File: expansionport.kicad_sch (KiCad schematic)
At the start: 18 parts, among them J20 C64_Expansion_Port, U31 74LS04, U32 74LVC374, U33 74LVC374, U34 74LVC374, U35 74LS374, U36 74LS374, U37 74LS374, U38 74LVC374, U39 74LVC374, U40 74LS374, U41 74LS374, U42 74LS06

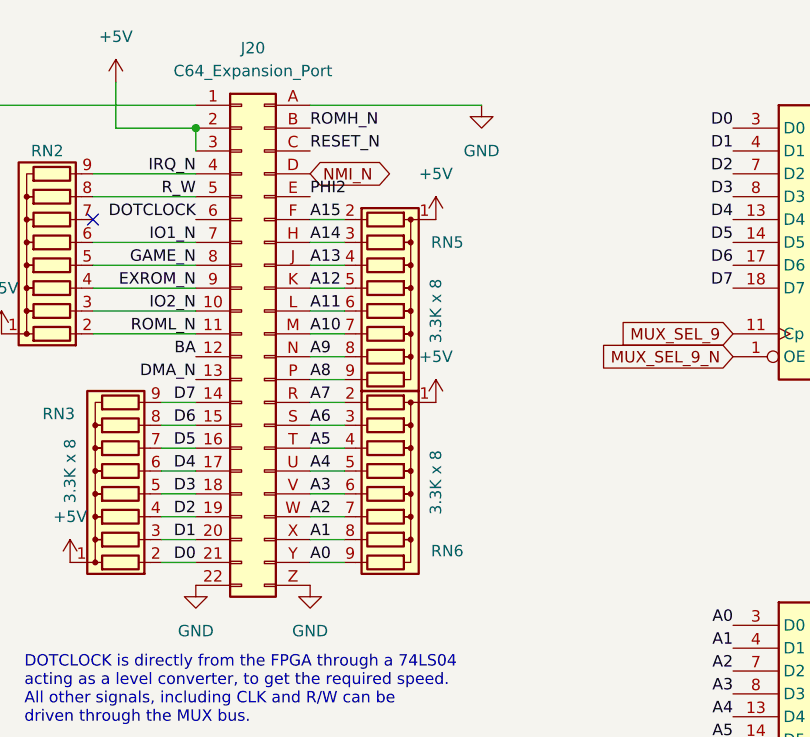
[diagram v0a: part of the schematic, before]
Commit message: route joystick ports and pullups etc
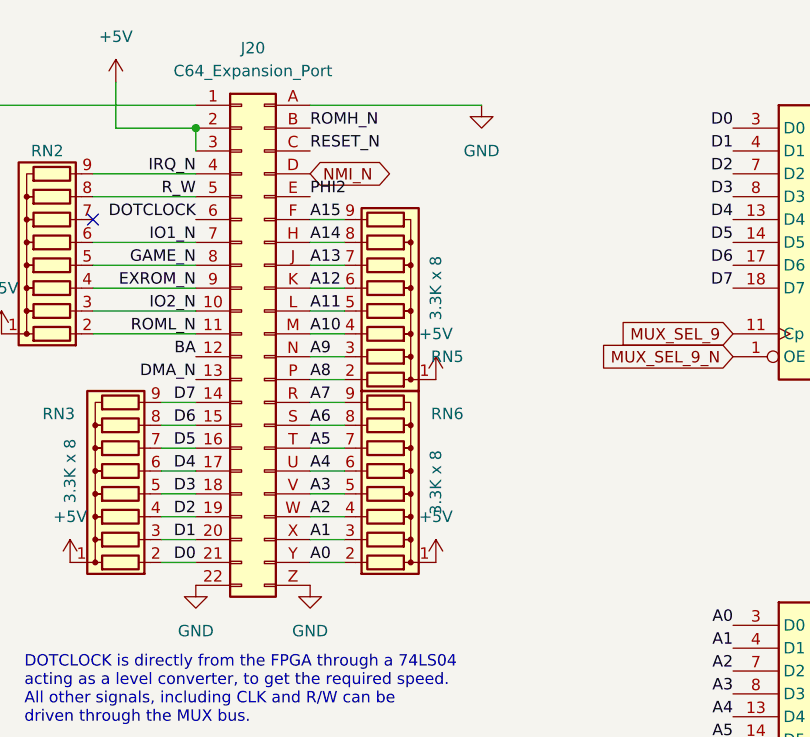
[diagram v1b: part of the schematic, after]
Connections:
- net A0: now also RN6.2 (R1); no longer RN6.9 (R8)
- net A1: now also RN6.3 (R2); no longer RN6.8 (R7)
- net A10: now also RN5.4 (R3); no longer RN5.7 (R6)
- net A11: now also RN5.5 (R4); no longer RN5.6 (R5)
- net A12: now also RN5.6 (R5); no longer RN5.5 (R4)
- net A13: now also RN5.7 (R6); no longer RN5.4 (R3)
- net A14: now also RN5.8 (R7); no longer RN5.3 (R2)
- net A15: now also RN5.9 (R8); no longer RN5.2 (R1)
- net A2: now also RN6.4 (R3); no longer RN6.7 (R6)
- net A3: now also RN6.5 (R4); no longer RN6.6 (R5)
- net A4: now also RN6.6 (R5); no longer RN6.5 (R4)
- net A5: now also RN6.7 (R6); no longer RN6.4 (R3)
- net A6: now also RN6.8 (R7); no longer RN6.3 (R2)
- net A7: now also RN6.9 (R8); no longer RN6.2 (R1)
- net A8: now also RN5.2 (R1); no longer RN5.9 (R8)
- net A9: now also RN5.3 (R2); no longer RN5.8 (R7)
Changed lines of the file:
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@@
     (pin "1")
   )
-  (symbol (lib_id "Device:R_Network08") (at 66.04 69.85 270) (unit 1)
+  (symbol (lib_id "Device:R_Network08") (at 66.04 67.31 270) (mirror x) (unit 1)
     (in_bom yes) (on_board yes)
-    (property "Reference" "RN6" (id 0) (at 72.39 76.2 90))
+    (property "Reference" "RN6" (id 0) (at 72.39 60.96 90))
     (property "Value" "3.3K x 8" (id 1) (at 71.12 68.58 0))
-    (property "Footprint" "Resistor_THT:R_Array_SIP9" (id 2) (at 66.04 81.915 90)
-      (effects (font (size 1.27 1.27)) hide)
-    )
-    (property "Datasheet" "http://www.vishay.com/docs/31509/csc.pdf" (id 3) (at 66.04 69.85 0)
+    (property "Footprint" "Resistor_THT:R_Array_SIP9" (id 2) (at 66.04 55.245 90)
+      (effects (font (size 1.27 1.27)) hide)
+    )
+    (property "Datasheet" "http://www.vishay.com/docs/31509/csc.pdf" (id 3) (at 66.04 67.31 0)
       (effects (font (size 1.27 1.27)) hide)
     )
@@
     (pin "Z")
   )
-  (symbol (lib_id "Device:R_Network08") (at 66.04 49.53 270) (unit 1)
+  (symbol (lib_id "Device:R_Network08") (at 66.04 46.99 270) (mirror x) (unit 1)
     (in_bom yes) (on_board yes)
-    (property "Reference" "RN5" (id 0) (at 72.39 41.91 90))
-    (property "Value" "3.3K x 8" (id 1) (at 71.12 49.53 0))
-    (property "Footprint" "Resistor_THT:R_Array_SIP9" (id 2) (at 66.04 61.595 90)
-      (effects (font (size 1.27 1.27)) hide)
-    )
-    (property "Datasheet" "http://www.vishay.com/docs/31509/csc.pdf" (id 3) (at 66.04 49.53 0)
+    (property "Reference" "RN5" (id 0) (at 72.39 54.61 90))
+    (property "Value" "3.3K x 8" (id 1) (at 71.12 46.99 0))
+    (property "Footprint" "Resistor_THT:R_Array_SIP9" (id 2) (at 66.04 34.925 90)
+      (effects (font (size 1.27 1.27)) hide)
+    )
+    (property "Datasheet" "http://www.vishay.com/docs/31509/csc.pdf" (id 3) (at 66.04 46.99 0)
       (effects (font (size 1.27 1.27)) hide)
     )
@@
     (pin "1")
   )
-  (symbol (lib_id "power:+5V") (at 71.12 59.69 0) (unit 1)
-    (in_bom yes) (on_board yes) (fields_autoplaced)
-    (property "Reference" "#PWR0238" (id 0) (at 71.12 63.5 0)
-      (effects (font (size 1.27 1.27)) hide)
-    )
-    (property "Value" "+5V" (id 1) (at 71.12 54.61 0))
-    (property "Footprint" "" (id 2) (at 71.12 59.69 0)
-      (effects (font (size 1.27 1.27)) hide)
-    )
-    (property "Datasheet" "" (id 3) (at 71.12 59.69 0)
+  (symbol (lib_id "power:+5V") (at 71.12 77.47 0) (unit 1)
+    (in_bom yes) (on_board yes) (fields_autoplaced)
+    (property "Reference" "#PWR0238" (id 0) (at 71.12 81.28 0)
+      (effects (font (size 1.27 1.27)) hide)
+    )
+    (property "Value" "+5V" (id 1) (at 71.12 72.39 0))
+    (property "Footprint" "" (id 2) (at 71.12 77.47 0)
+      (effects (font (size 1.27 1.27)) hide)
+    )
+    (property "Datasheet" "" (id 3) (at 71.12 77.47 0)
       (effects (font (size 1.27 1.27)) hide)
     )
@@
     (pin "1")
   )
-  (symbol (lib_id "power:+5V") (at 71.12 39.37 0) (unit 1)
-    (in_bom yes) (on_board yes) (fields_autoplaced)
-    (property "Reference" "#PWR0248" (id 0) (at 71.12 43.18 0)
-      (effects (font (size 1.27 1.27)) hide)
-    )
-    (property "Value" "+5V" (id 1) (at 71.12 34.29 0))
-    (property "Footprint" "" (id 2) (at 71.12 39.37 0)
-      (effects (font (size 1.27 1.27)) hide)
-    )
-    (property "Datasheet" "" (id 3) (at 71.12 39.37 0)
-      (effects (font (size 1.27 1.27)) hide)
-    )
+  (symbol (lib_id "power:+5V") (at 71.12 57.15 0) (unit 1)
+    (in_bom yes) (on_board yes) (fields_autoplaced)
+    (property "Reference" "#PWR0248" (id 0) (at 71.12 60.96 0)
+      (effects (font (size 1.27 1.27)) hide)
+    )
+    (property "Value" "+5V" (id 1) (at 71.12 52.07 0))
+    (property "Footprint" "" (id 2) (at 71.12 57.15 0)
+      (effects (font (size 1.27 1.27)) hide)
+    )
+    (property "Datasheet" "" (id 3) (at 71.12 57.15 0)
+      (effects (font (size 1.27 1.27)) hide)
+    )

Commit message: add missing footprints
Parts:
- U42: footprint (none) -> Package_DIP:DIP-14_W7.62mm
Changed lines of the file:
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@@
       (effects (font (size 1.27 1.27)) (justify left))
     )
-    (property "Footprint" "" (id 2) (at 19.05 176.53 0)
+    (property "Footprint" "Package_DIP:DIP-14_W7.62mm" (id 2) (at 19.05 176.53 0)
       (effects (font (size 1.27 1.27)) hide)
     )
@@
     (property "Reference" "U42" (id 0) (at 45.085 179.07 0))
     (property "Value" "74LS06" (id 1) (at 45.085 181.61 0))
-    (property "Footprint" "" (id 2) (at 45.085 187.96 0)
+    (property "Footprint" "Package_DIP:DIP-14_W7.62mm" (id 2) (at 45.085 187.96 0)
       (effects (font (size 1.27 1.27)) hide)
     )
@@
     (property "Reference" "U42" (id 0) (at 90.805 167.64 0))
     (property "Value" "74LS06" (id 1) (at 90.805 170.18 0))
-    (property "Footprint" "" (id 2) (at 90.805 177.165 0)
+    (property "Footprint" "Package_DIP:DIP-14_W7.62mm" (id 2) (at 90.805 177.165 0)
       (effects (font (size 1.27 1.27)) hide)
     )
@@
     (property "Reference" "U42" (id 0) (at 90.805 179.07 0))
     (property "Value" "74LS06" (id 1) (at 90.805 181.61 0))
-    (property "Footprint" "" (id 2) (at 90.805 187.96 0)
+    (property "Footprint" "Package_DIP:DIP-14_W7.62mm" (id 2) (at 90.805 187.96 0)
       (effects (font (size 1.27 1.27)) hide)
     )
@@
     (property "Reference" "U42" (id 0) (at 41.91 151.765 0))
     (property "Value" "74LS06" (id 1) (at 41.91 154.305 0))
-    (property "Footprint" "" (id 2) (at 41.91 161.29 0)
+    (property "Footprint" "Package_DIP:DIP-14_W7.62mm" (id 2) (at 41.91 161.29 0)
       (effects (font (size 1.27 1.27)) hide)
     )
@@
     (property "Reference" "U42" (id 0) (at 138.43 179.07 0))
     (property "Value" "74LS06" (id 1) (at 138.43 181.61 0))
-    (property "Footprint" "" (id 2) (at 138.43 187.96 0)
+    (property "Footprint" "Package_DIP:DIP-14_W7.62mm" (id 2) (at 138.43 187.96 0)
       (effects (font (size 1.27 1.27)) hide)
     )
@@
     (property "Reference" "U42" (id 0) (at 138.43 167.64 0))
     (property "Value" "74LS06" (id 1) (at 138.43 170.18 0))
-    (property "Footprint" "" (id 2) (at 138.43 177.165 0)
-      (effects (font (size 1.27 1.27)) hide)
-    )
+    (property "Footprint" "Package_DIP:DIP-14_W7.62mm" (id 2) (at 138.43 177.165 0)
+      (effects (font (size 1.27 1.27)) hide)
+    )

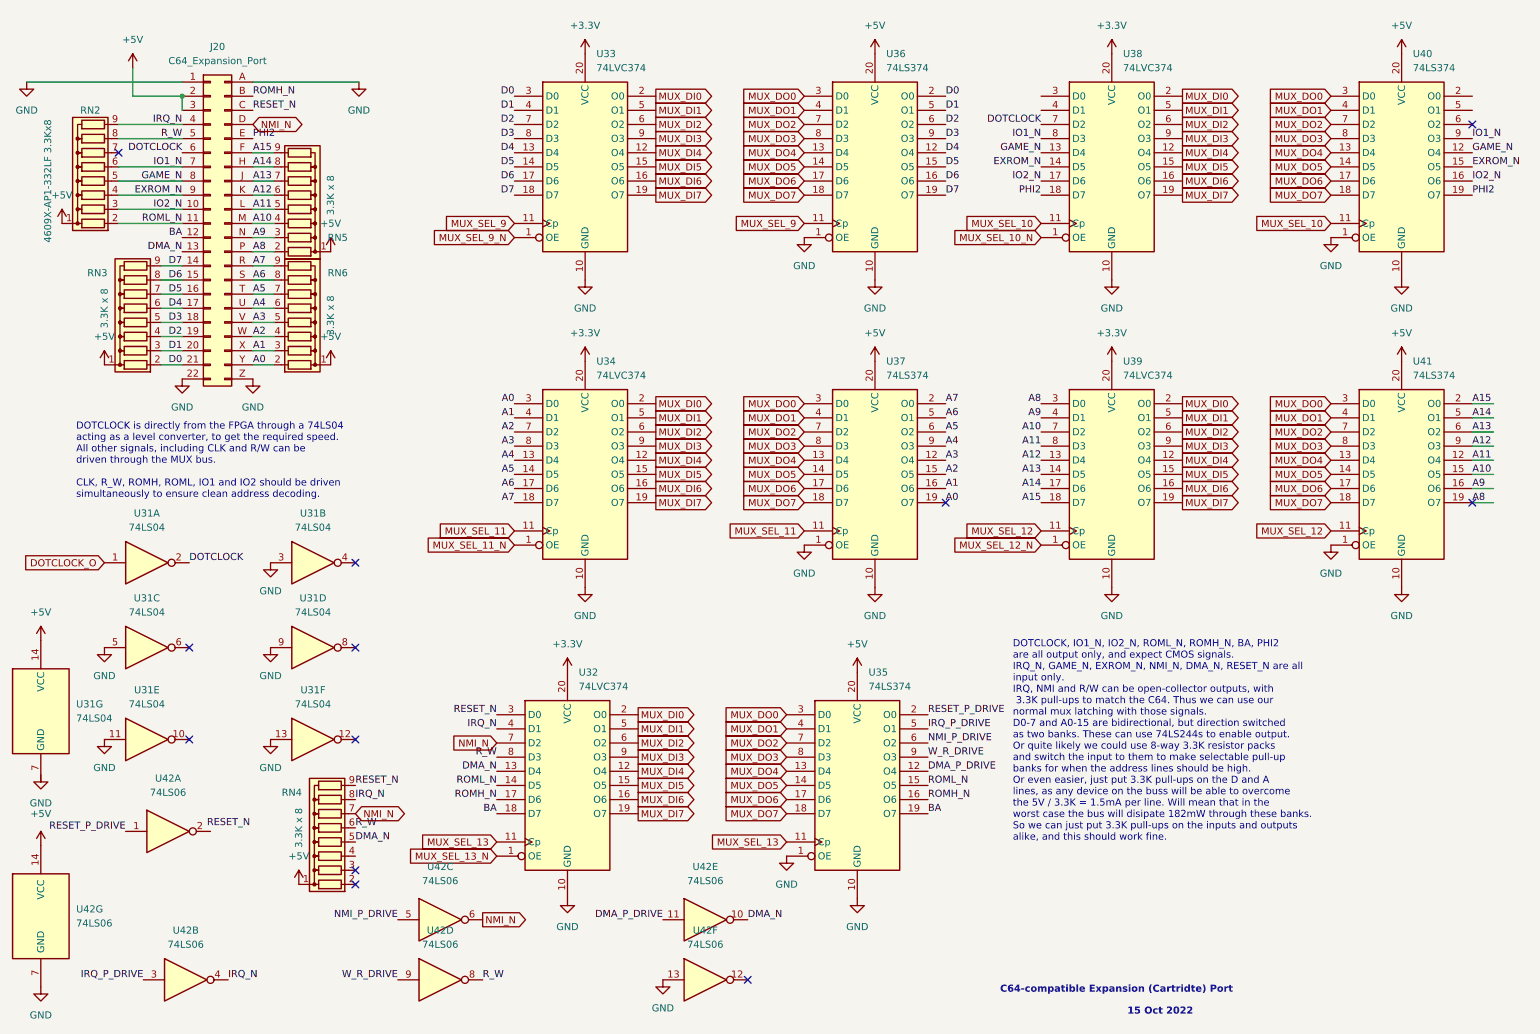
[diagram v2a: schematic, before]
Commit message: route cart port to resistor packs
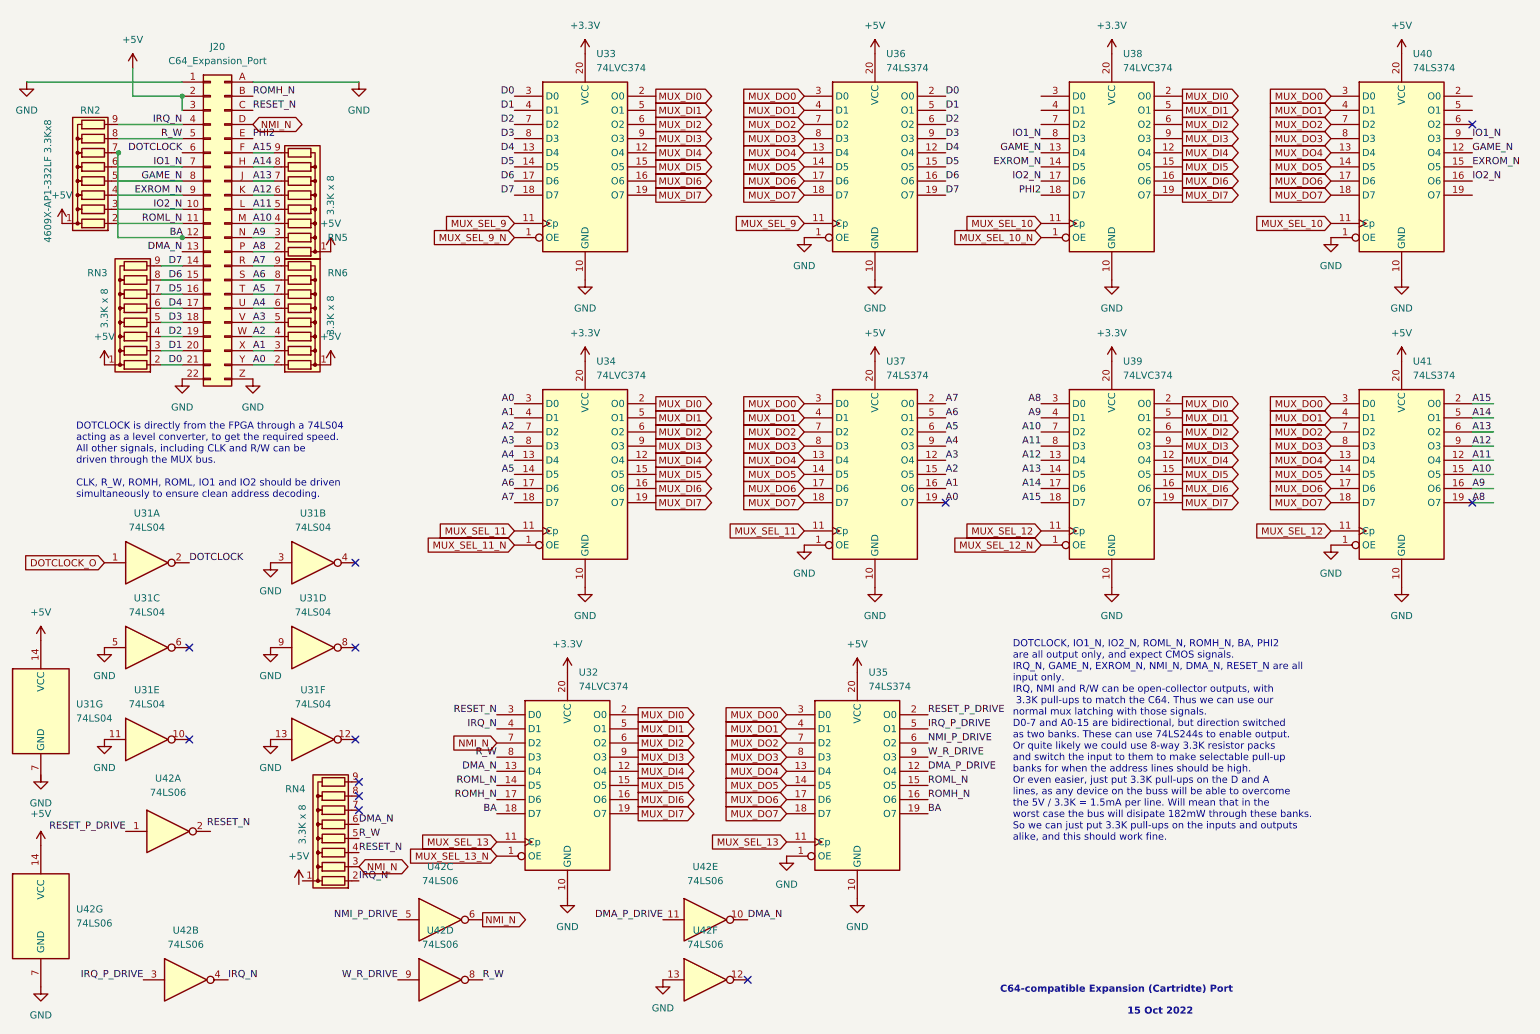
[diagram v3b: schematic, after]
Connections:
- net +5V: no longer RN4.1 (common)
- net BA: now also RN2.7 (R6)
- net DMA_N: now also RN4.6 (R5); no longer RN4.5 (R4)
- net DOTCLOCK: no longer U38.7 (D2)
- net IRQ_N: now also RN4.2 (R1); no longer RN4.8 (R7)
- net NMI_N: now also RN4.3 (R2); no longer RN4.7 (R6)
- net PHI2: no longer U40.19 (O7)
- net RESET_N: now also RN4.4 (R3); no longer RN4.9 (R8)
- net R_W: now also RN4.5 (R4); no longer RN4.6 (R5)
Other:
- moved on the sheet: RN4
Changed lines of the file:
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@@
 (kicad_sch (version 20211123) (generator eeschema)
   (paper "A4")
+  (junction (at 44.45 54.61) (diameter 0) (color 0 0 0 0)
+  )
+  (junction (at 33.02 39.37) (diameter 0) (color 0 0 0 0)
+  )
   (junction (at 44.45 29.21) (diameter 0) (color 0 0 0 0)
   )
-  (no_connect (at 33.02 39.37))
   (no_connect (at 181.61 102.235))
+  (no_connect (at 76.2 154.94))
   (no_connect (at 75.565 128.27))
   (no_connect (at 276.225 34.29))
+  (no_connect (at 76.2 152.4))
   (no_connect (at 75.565 113.03))
   (no_connect (at 75.565 144.78))
   (no_connect (at 45.72 128.27))
-  (no_connect (at 75.565 170.815))
   (no_connect (at 146.05 187.96))
+  (no_connect (at 76.2 157.48))
   (no_connect (at 276.225 102.235))
-  (no_connect (at 75.565 168.275))
   (no_connect (at 45.72 144.78))
   (wire (pts (xy 40.64 59.69) (xy 44.45 59.69))
@@
     (stroke (width 0) (type default) (color 0 0 0 0))
   )
+  (wire (pts (xy 32.893 54.61) (xy 44.45 54.61))
+    (stroke (width 0) (type default) (color 0 0 0 0))
+  )
+  (wire (pts (xy 44.45 54.61) (xy 44.577 54.61))
+    (stroke (width 0) (type default) (color 0 0 0 0))
+  )
   (wire (pts (xy 40.64 74.93) (xy 44.45 74.93))
     (stroke (width 0) (type default) (color 0 0 0 0))
@@
     (stroke (width 0) (type default) (color 0 0 0 0))
   )
+  (wire (pts (xy 32.893 39.37) (xy 32.893 54.61))
+    (stroke (width 0) (type default) (color 0 0 0 0))
+  )
   (wire (pts (xy 40.64 77.47) (xy 44.45 77.47))
     (stroke (width 0) (type default) (color 0 0 0 0))
@@
   )
   (wire (pts (xy 276.225 94.615) (xy 280.035 94.615))
+    (stroke (width 0) (type default) (color 0 0 0 0))
+  )
+  (wire (pts (xy 32.893 39.37) (xy 33.02 39.37))
     (stroke (width 0) (type default) (color 0 0 0 0))
   )
@@
     (effects (font (size 1.27 1.27)) (justify left bottom))
   )
-  (label "PHI2" (at 276.225 46.99 0)
-    (effects (font (size 1.27 1.27)) (justify left bottom))
-  )
   (label "A4" (at 57.15 67.31 0)
     (effects (font (size 1.27 1.27)) (justify left bottom))
@@
     (effects (font (size 1.27 1.27)) (justify right bottom))
   )
-  (label "BA" (at 44.45 54.61 180)
+  (label "BA" (at 44.577 54.61 180)
     (effects (font (size 1.27 1.27)) (justify right bottom))
   )
@@
     (effects (font (size 1.27 1.27)) (justify right bottom))
   )
-  (label "RESET_N" (at 75.565 153.035 0)
+  (label "RESET_N" (at 76.2 165.1 0)
     (effects (font (size 1.27 1.27)) (justify left bottom))
   )
@@
     (effects (font (size 1.27 1.27)) (justify right bottom))
   )
-  (label "R_W" (at 75.565 160.655 0)
+  (label "R_W" (at 76.2 162.56 0)
     (effects (font (size 1.27 1.27)) (justify left bottom))
   )
@@
     (effects (font (size 1.27 1.27)) (justify left bottom))
   )
-  (label "IRQ_N" (at 75.565 155.575 0)
+  (label "IRQ_N" (at 76.2 170.18 0)
     (effects (font (size 1.27 1.27)) (justify left bottom))
   )
@@
     (effects (font (size 1.27 1.27)) (justify right bottom))
   )
-  (label "DOTCLOCK" (at 198.755 34.29 180)
-    (effects (font (size 1.27 1.27)) (justify right bottom))
-  )
   (label "GAME_N" (at 198.755 39.37 180)
     (effects (font (size 1.27 1.27)) (justify right bottom))
@@
     (effects (font (size 1.27 1.27)) (justify left bottom))
   )
-  (label "DMA_N" (at 75.565 163.195 0)
+  (label "DMA_N" (at 76.2 160.02 0)
     (effects (font (size 1.27 1.27)) (justify left bottom))
   )
@@
     )
   )
-  (global_label "NMI_N" (shape bidirectional) (at 75.565 158.115 0) (fields_autoplaced)
-    (effects (font (size 1.27 1.27)) (justify left))
-    (property "Intersheet References" "${INTERSHEET_REFS}" (id 0) (at 83.6629 158.0356 0)
+  (global_label "NMI_N" (shape bidirectional) (at 76.2 167.64 0) (fields_autoplaced)
+    (effects (font (size 1.27 1.27)) (justify left))
+    (property "Intersheet References" "${INTERSHEET_REFS}" (id 0) (at 84.2979 167.5606 0)
       (effects (font (size 1.27 1.27)) (justify left) hide)
     )
@@
     (pin "1")
   )
-  (symbol (lib_id "Device:R_Network08") (at 70.485 160.655 90) (unit 1)
+  (symbol (lib_id "Device:R_Network08") (at 71.12 160.02 90) (unit 1)
     (in_bom yes) (on_board yes)
-    (property "Reference" "RN4" (id 0) (at 64.135 154.305 90))
-    (property "Value" "3.3K x 8" (id 1) (at 65.405 160.655 0))
-    (property "Footprint" "Resistor_THT:R_Array_SIP9" (id 2) (at 70.485 148.59 90)
-      (effects (font (size 1.27 1.27)) hide)
-    )
-    (property "Datasheet" "http://www.vishay.com/docs/31509/csc.pdf" (id 3) (at 70.485 160.655 0)
-      (effects (font (size 1.27 1.27)) hide)
-    )
+    (property "Reference" "RN4" (id 0) (at 64.77 153.67 90))
+    (property "Value" "3.3K x 8" (id 1) (at 66.04 160.02 0))
+    (property "Footprint" "Resistor_THT:R_Array_SIP9" (id 2) (at 71.12 147.955 90)
+      (effects (font (size 1.27 1.27)) hide)
+    )
+    (property "Datasheet" "http://www.vishay.com/docs/31509/csc.pdf" (id 3) (at 71.12 160.02 0)
+      (effects (font (size 1.27 1.27)) hide)
+    )
